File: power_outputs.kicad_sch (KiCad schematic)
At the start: 10 parts, among them Q1 BSS138, Q3 MMBT3904, Q4 MMBT3906

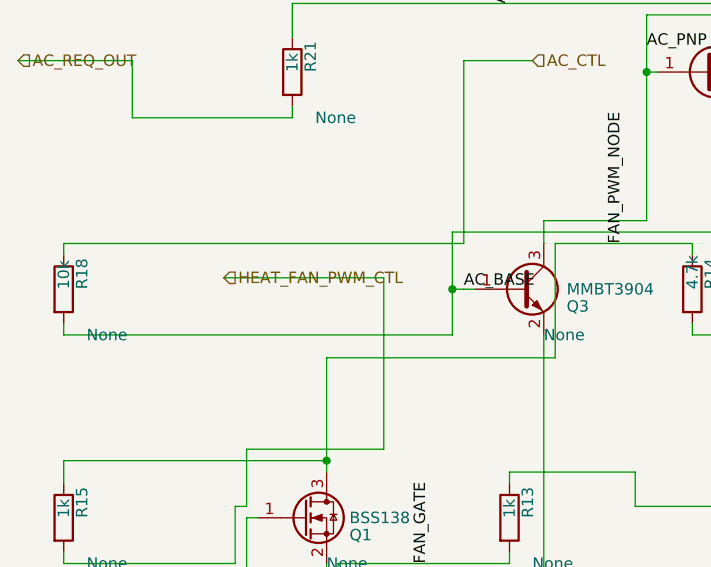
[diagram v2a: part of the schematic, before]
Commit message: optimazed load to kicad
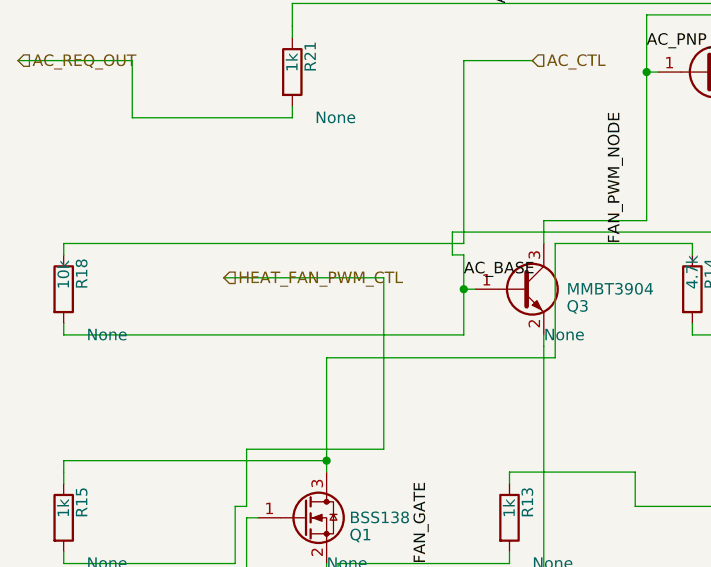
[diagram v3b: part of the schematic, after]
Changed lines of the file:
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@@
 		(instances
 			(project "Untitled"
-				(path "/1e88dd50-46bb-44a6-af8a-a123738594cb"
+				(path "/90d6963e-6ac5-4f32-9aa0-e0ee6a940a9b"
 					(reference "Q1")
 					(unit 1)
@@
 		(instances
 			(project "Untitled"
-				(path "/1e88dd50-46bb-44a6-af8a-a123738594cb"
+				(path "/90d6963e-6ac5-4f32-9aa0-e0ee6a940a9b"
 					(reference "Q3")
 					(unit 1)
@@
 		(instances
 			(project "Untitled"
-				(path "/1e88dd50-46bb-44a6-af8a-a123738594cb"
+				(path "/90d6963e-6ac5-4f32-9aa0-e0ee6a940a9b"
 					(reference "Q4")
 					(unit 1)
@@
 		(instances
 			(project "Untitled"
-				(path "/1e88dd50-46bb-44a6-af8a-a123738594cb"
+				(path "/90d6963e-6ac5-4f32-9aa0-e0ee6a940a9b"
 					(reference "R13")
 					(unit 1)
@@
 		(instances
 			(project "Untitled"
-				(path "/1e88dd50-46bb-44a6-af8a-a123738594cb"
+				(path "/90d6963e-6ac5-4f32-9aa0-e0ee6a940a9b"
 					(reference "R14")
 					(unit 1)
@@
 		(instances
 			(project "Untitled"
-				(path "/1e88dd50-46bb-44a6-af8a-a123738594cb"
+				(path "/90d6963e-6ac5-4f32-9aa0-e0ee6a940a9b"
 					(reference "R15")
 					(unit 1)
@@
 		(instances
 			(project "Untitled"
-				(path "/1e88dd50-46bb-44a6-af8a-a123738594cb"
+				(path "/90d6963e-6ac5-4f32-9aa0-e0ee6a940a9b"
 					(reference "R18")
 					(unit 1)
@@
 		(instances
 			(project "Untitled"
-				(path "/1e88dd50-46bb-44a6-af8a-a123738594cb"
+				(path "/90d6963e-6ac5-4f32-9aa0-e0ee6a940a9b"
 					(reference "R19")
 					(unit 1)
@@
 		(instances
 			(project "Untitled"
-				(path "/1e88dd50-46bb-44a6-af8a-a123738594cb"
+				(path "/90d6963e-6ac5-4f32-9aa0-e0ee6a940a9b"
 					(reference "R20")
 					(unit 1)
@@
 		(instances
 			(project "Untitled"
-				(path "/1e88dd50-46bb-44a6-af8a-a123738594cb"
+				(path "/90d6963e-6ac5-4f32-9aa0-e0ee6a940a9b"
 					(reference "R21")
 					(unit 1)
@@
 	(wire
 		(pts
-			(xy 53.34 33.02) (xy 52.07 33.02)
-		)
-		(stroke
-			(width 0)
-			(type default)
-		)
-	)
-	(wire
-		(pts
-			(xy 52.07 33.02) (xy 52.07 26.67)
+			(xy 53.34 33.02) (xy 53.34 29.21)
+		)
+		(stroke
+			(width 0)
+			(type default)
+		)
+	)
+	(wire
+		(pts
+			(xy 53.34 29.21) (xy 52.07 29.21)
+		)
+		(stroke
+			(width 0)
+			(type default)
+		)
+	)
+	(wire
+		(pts
+			(xy 52.07 29.21) (xy 52.07 26.67)
 		)
 		(stroke
@@
 	(wire
 		(pts
-			(xy 8.89 38.1) (xy 52.07 38.1)
-		)
-		(stroke
-			(width 0)
-			(type default)
-		)
-	)
-	(wire
-		(pts
-			(xy 52.07 38.1) (xy 52.07 33.02)
+			(xy 8.89 38.1) (xy 53.34 38.1)
+		)
+		(stroke
+			(width 0)
+			(type default)
+		)
+	)
+	(wire
+		(pts
+			(xy 53.34 38.1) (xy 53.34 33.02)
 		)
 		(stroke
@@
 	)
 	(junction
-		(at 52.07 33.02)
+		(at 53.34 33.02)
 		(diameter 0)
 		(color 0 0 0 0)
@@
 	)
 	(label "AC_BASE"
-		(at 53.34 33.02 180)
+		(at 53.34 31.75 180)
 		(effects
 			(font

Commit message: tests_fix
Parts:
- Q1, Q3, Q4, R13, R14, R15, R18, R19, R20, R21: hierarchy_path (none) -> /c5a034c1-1f54-4e7e-8711-0930d2b4314e/a70dfe10-e340-4dc2-93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
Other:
- title: (none) -> climate_control_niva_travel
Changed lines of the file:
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@@
 	(generator_version "9.0")
 	(paper "A4")
+	(title_block
+		(title "climate_control_niva_travel")
+	)
 	(symbol
 		(lib_id "Transistor_FET:BSS138")
@@
 			)
 		)
+		(property "hierarchy_path" "/c5a034c1-1f54-4e7e-8711-0930d2b4314e/a70dfe10-e340-4dc2-93bf-45c80fe91fa7"
+			(at 38.1 63.4999 0)
+			(effects
+				(font
+					(size 1.27 1.27)
+				)
+				(justify left)
+			)
+		)
 		(pin "1"
 		)
@@
 		)
 		(instances
-			(project "Untitled"
-				(path "/90d6963e-6ac5-4f32-9aa0-e0ee6a940a9b"
+			(project "climate_control_niva_travel"
+				(path "/c5a034c1-1f54-4e7e-8711-0930d2b4314e/a70dfe10-e340-4dc2-93bf-45c80fe91fa7"
 					(reference "Q1")
 					(unit 1)
@@
 			)
 		)
+		(property "hierarchy_path" "/c5a034c1-1f54-4e7e-8711-0930d2b4314e/a70dfe10-e340-4dc2-93bf-45c80fe91fa7"
+			(at 62.23 38.0999 0)
+			(effects
+				(font
+					(size 1.27 1.27)
+				)
+				(justify left)
+			)
+		)
 		(pin "1"
 		)
@@
 		)
 		(instances
-			(project "Untitled"
-				(path "/90d6963e-6ac5-4f32-9aa0-e0ee6a940a9b"
+			(project "climate_control_niva_travel"
+				(path "/c5a034c1-1f54-4e7e-8711-0930d2b4314e/a70dfe10-e340-4dc2-93bf-45c80fe91fa7"
 					(reference "Q3")
 					(unit 1)
@@
 			)
 		)
+		(property "hierarchy_path" "/c5a034c1-1f54-4e7e-8711-0930d2b4314e/a70dfe10-e340-4dc2-93bf-45c80fe91fa7"
+			(at 82.55 13.9699 0)
+			(effects
+				(font
+					(size 1.27 1.27)
+				)
+				(justify left)
+			)
+		)
 		(pin "1"
 		)
@@
 		)
 		(instances
-			(project "Untitled"
-				(path "/90d6963e-6ac5-4f32-9aa0-e0ee6a940a9b"
+			(project "climate_control_niva_travel"
+				(path "/c5a034c1-1f54-4e7e-8711-0930d2b4314e/a70dfe10-e340-4dc2-93bf-45c80fe91fa7"
 					(reference "Q4")
 					(unit 1)
@@
 			)
 		)
+		(property "hierarchy_path" "/c5a034c1-1f54-4e7e-8711-0930d2b4314e/a70dfe10-e340-4dc2-93bf-45c80fe91fa7"
+			(at 60.96 63.4999 0)
+			(effects
+				(font
+					(size 1.27 1.27)
+				)
+				(justify left)
+			)
+		)
 		(pin "1"
 		)
@@
 		)
 		(instances
-			(project "Untitled"
-				(path "/90d6963e-6ac5-4f32-9aa0-e0ee6a940a9b"
+			(project "climate_control_niva_travel"
+				(path "/c5a034c1-1f54-4e7e-8711-0930d2b4314e/a70dfe10-e340-4dc2-93bf-45c80fe91fa7"
 					(reference "R13")
 					(unit 1)
@@
 			)
 		)
+		(property "hierarchy_path" "/c5a034c1-1f54-4e7e-8711-0930d2b4314e/a70dfe10-e340-4dc2-93bf-45c80fe91fa7"
+			(at 81.28 38.0999 0)
+			(effects
+				(font
+					(size 1.27 1.27)
+				)
+				(justify left)
+			)
+		)
 		(pin "1"
 		)
@@
 		)
 		(instances
-			(project "Untitled"
-				(path "/90d6963e-6ac5-4f32-9aa0-e0ee6a940a9b"
+			(project "climate_control_niva_travel"
+				(path "/c5a034c1-1f54-4e7e-8711-0930d2b4314e/a70dfe10-e340-4dc2-93bf-45c80fe91fa7"
 					(reference "R14")
 					(unit 1)
@@
 			)
 		)
+		(property "hierarchy_path" "/c5a034c1-1f54-4e7e-8711-0930d2b4314e/a70dfe10-e340-4dc2-93bf-45c80fe91fa7"
+			(at 11.43 63.4999 0)
+			(effects
+				(font
+					(size 1.27 1.27)
+				)
+				(justify left)
+			)
+		)
 		(pin "1"
 		)
@@
 		)
 		(instances
-			(project "Untitled"
-				(path "/90d6963e-6ac5-4f32-9aa0-e0ee6a940a9b"
+			(project "climate_control_niva_travel"
+				(path "/c5a034c1-1f54-4e7e-8711-0930d2b4314e/a70dfe10-e340-4dc2-93bf-45c80fe91fa7"
 					(reference "R15")
 					(unit 1)
@@
 			)
 		)
+		(property "hierarchy_path" "/c5a034c1-1f54-4e7e-8711-0930d2b4314e/a70dfe10-e340-4dc2-93bf-45c80fe91fa7"
+			(at 11.43 38.0999 0)
+			(effects
+				(font
+					(size 1.27 1.27)
+				)
+				(justify left)
+			)
+		)
 		(pin "1"
 		)
@@
 		)
 		(instances
-			(project "Untitled"
-				(path "/90d6963e-6ac5-4f32-9aa0-e0ee6a940a9b"
+			(project "climate_control_niva_travel"
+				(path "/c5a034c1-1f54-4e7e-8711-0930d2b4314e/a70dfe10-e340-4dc2-93bf-45c80fe91fa7"
 					(reference "R18")
 					(unit 1)
@@
 			)
 		)
+		(property "hierarchy_path" "/c5a034c1-1f54-4e7e-8711-0930d2b4314e/a70dfe10-e340-4dc2-93bf-45c80fe91fa7"
+			(at 100.33 38.0999 0)
+			(effects
+				(font
+					(size 1.27 1.27)
+				)
+				(justify left)
+			)
+		)
 		(pin "1"
 		)
@@
 		)
 		(instances
-			(project "Untitled"
-				(path "/90d6963e-6ac5-4f32-9aa0-e0ee6a940a9b"
+			(project "climate_control_niva_travel"
+				(path "/c5a034c1-1f54-4e7e-8711-0930d2b4314e/a70dfe10-e340-4dc2-93bf-45c80fe91fa7"
 					(reference "R19")
 					(unit 1)
@@
 			)
 		)
+		(property "hierarchy_path" "/c5a034c1-1f54-4e7e-8711-0930d2b4314e/a70dfe10-e340-4dc2-93bf-45c80fe91fa7"
+			(at 100.33 13.9699 0)
+			(effects
+				(font
+					(size 1.27 1.27)
+				)
+				(justify left)
+			)
+		)
 		(pin "1"
 		)
@@
 		)
 		(instances
-			(project "Untitled"
-				(path "/90d6963e-6ac5-4f32-9aa0-e0ee6a940a9b"
+			(project "climate_control_niva_travel"
+				(path "/c5a034c1-1f54-4e7e-8711-0930d2b4314e/a70dfe10-e340-4dc2-93bf-45c80fe91fa7"
 					(reference "R20")
 					(unit 1)
@@
 			)
 		)
+		(property "hierarchy_path" "/c5a034c1-1f54-4e7e-8711-0930d2b4314e/a70dfe10-e340-4dc2-93bf-45c80fe91fa7"
+			(at 36.83 13.9699 0)
+			(effects
+				(font
+					(size 1.27 1.27)
+				)
+				(justify left)
+			)
+		)
 		(pin "1"
 		)
@@
 		)
 		(instances
-			(project "Untitled"
-				(path "/90d6963e-6ac5-4f32-9aa0-e0ee6a940a9b"
+			(project "climate_control_niva_travel"
+				(path "/c5a034c1-1f54-4e7e-8711-0930d2b4314e/a70dfe10-e340-4dc2-93bf-45c80fe91fa7"
 					(reference "R21")
 					(unit 1)
@@
 	(junction
 		(at 73.66 8.89)
+		(diameter 0)
+		(color 0 0 0 0)
+	)
+	(junction
+		(at 49.53 63.5)
+		(diameter 0)
+		(color 0 0 0 0)
+	)
+	(junction
+		(at 71.12 27.94)
+		(diameter 0)
+		(color 0 0 0 0)
+	)
+	(junction
+		(at 53.34 31.75)
+		(diameter 0)
+		(color 0 0 0 0)
+	)
+	(junction
+		(at 73.66 6.35)
+		(diameter 0)
+		(color 0 0 0 0)
+	)
+	(junction
+		(at 58.42 1.27)
 		(diameter 0)
 		(color 0 0 0 0)
@@
 	)
 	(hierarchical_label "AC_REQ_OUT"
-		(shape input)
+		(shape output)
 		(at 3.81 7.62 0)
 		(effects
@@
 	)
 	(hierarchical_label "HEAT_FAN_PWM_CTL"
-		(shape input)
+		(shape output)
 		(at 26.67 31.75 0)
 		(effects

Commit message: refactoring
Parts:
- Q1, Q3, Q4, R13, R14, R15, R18, R19, R20, R21: hierarchy_path /c5a034c1-1f54-4e7e-8711-0930d2b4314e/a70dfe10-e340-4dc2-93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 -> (none)
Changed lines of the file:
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@@
-			)
-		)
-		(property "hierarchy_path" "/c5a034c1-1f54-4e7e-8711-0930d2b4314e/a70dfe10-e340-4dc2-93bf-45c80fe91fa7"
-			(at 38.1 63.4999 0)
-			(effects
-				(font
-					(size 1.27 1.27)
-				)
-				(justify left)
 			)
 		)
@@
 		(instances
 			(project "climate_control_niva_travel"
-				(path "/c5a034c1-1f54-4e7e-8711-0930d2b4314e/a70dfe10-e340-4dc2-93bf-45c80fe91fa7"
-					(reference "Q1")
+				(path "/165a98f1-2dde-4141-9fdc-c935d39c8cff/176bfc83-1f39-4dbb-bd36-1c3de8b994cb/"
+					(reference "Q0701")
 					(unit 1)
 				)
@@
 			)
 		)
-		(property "hierarchy_path" "/c5a034c1-1f54-4e7e-8711-0930d2b4314e/a70dfe10-e340-4dc2-93bf-45c80fe91fa7"
-			(at 62.23 38.0999 0)
-			(effects
-				(font
-					(size 1.27 1.27)
-				)
-				(justify left)
-			)
-		)
 		(pin "1"
 		)
@@
 		(instances
 			(project "climate_control_niva_travel"
-				(path "/c5a034c1-1f54-4e7e-8711-0930d2b4314e/a70dfe10-e340-4dc2-93bf-45c80fe91fa7"
-					(reference "Q3")
+				(path "/165a98f1-2dde-4141-9fdc-c935d39c8cff/176bfc83-1f39-4dbb-bd36-1c3de8b994cb/"
+					(reference "Q0703")
 					(unit 1)
 				)
@@
 			)
 		)
-		(property "hierarchy_path" "/c5a034c1-1f54-4e7e-8711-0930d2b4314e/a70dfe10-e340-4dc2-93bf-45c80fe91fa7"
-			(at 82.55 13.9699 0)
-			(effects
-				(font
-					(size 1.27 1.27)
-				)
-				(justify left)
-			)
-		)
 		(pin "1"
 		)
@@
 		(instances
 			(project "climate_control_niva_travel"
-				(path "/c5a034c1-1f54-4e7e-8711-0930d2b4314e/a70dfe10-e340-4dc2-93bf-45c80fe91fa7"
-					(reference "Q4")
+				(path "/165a98f1-2dde-4141-9fdc-c935d39c8cff/176bfc83-1f39-4dbb-bd36-1c3de8b994cb/"
+					(reference "Q0704")
 					(unit 1)
 				)
@@
 			)
 		)
-		(property "hierarchy_path" "/c5a034c1-1f54-4e7e-8711-0930d2b4314e/a70dfe10-e340-4dc2-93bf-45c80fe91fa7"
-			(at 60.96 63.4999 0)
-			(effects
-				(font
-					(size 1.27 1.27)
-				)
-				(justify left)
-			)
-		)
-		(pin "1"
-		)
-		(pin "2"
-		)
-		(instances
-			(project "climate_control_niva_travel"
-				(path "/c5a034c1-1f54-4e7e-8711-0930d2b4314e/a70dfe10-e340-4dc2-93bf-45c80fe91fa7"
-					(reference "R13")
+		(pin "1"
+		)
+		(pin "2"
+		)
+		(instances
+			(project "climate_control_niva_travel"
+				(path "/165a98f1-2dde-4141-9fdc-c935d39c8cff/176bfc83-1f39-4dbb-bd36-1c3de8b994cb/"
+					(reference "R0713")
 					(unit 1)
 				)
@@
 			)
 		)
-		(property "hierarchy_path" "/c5a034c1-1f54-4e7e-8711-0930d2b4314e/a70dfe10-e340-4dc2-93bf-45c80fe91fa7"
-			(at 81.28 38.0999 0)
-			(effects
-				(font
-					(size 1.27 1.27)
-				)
-				(justify left)
-			)
-		)
-		(pin "1"
-		)
-		(pin "2"
-		)
-		(instances
-			(project "climate_control_niva_travel"
-				(path "/c5a034c1-1f54-4e7e-8711-0930d2b4314e/a70dfe10-e340-4dc2-93bf-45c80fe91fa7"
-					(reference "R14")
+		(pin "1"
+		)
+		(pin "2"
+		)
+		(instances
+			(project "climate_control_niva_travel"
+				(path "/165a98f1-2dde-4141-9fdc-c935d39c8cff/176bfc83-1f39-4dbb-bd36-1c3de8b994cb/"
+					(reference "R0714")
 					(unit 1)
 				)
@@
 			)
 		)
-		(property "hierarchy_path" "/c5a034c1-1f54-4e7e-8711-0930d2b4314e/a70dfe10-e340-4dc2-93bf-45c80fe91fa7"
-			(at 11.43 63.4999 0)
-			(effects
-				(font
-					(size 1.27 1.27)
-				)
-				(justify left)
-			)
-		)
-		(pin "1"
-		)
-		(pin "2"
-		)
-		(instances
-			(project "climate_control_niva_travel"
-				(path "/c5a034c1-1f54-4e7e-8711-0930d2b4314e/a70dfe10-e340-4dc2-93bf-45c80fe91fa7"
-					(reference "R15")
+		(pin "1"
+		)
+		(pin "2"
+		)
+		(instances
+			(project "climate_control_niva_travel"
+				(path "/165a98f1-2dde-4141-9fdc-c935d39c8cff/176bfc83-1f39-4dbb-bd36-1c3de8b994cb/"
+					(reference "R0715")
 					(unit 1)
 				)
@@
 			)
 		)
-		(property "hierarchy_path" "/c5a034c1-1f54-4e7e-8711-0930d2b4314e/a70dfe10-e340-4dc2-93bf-45c80fe91fa7"
-			(at 11.43 38.0999 0)
-			(effects
-				(font
-					(size 1.27 1.27)
-				)
-				(justify left)
-			)
-		)
-		(pin "1"
-		)
-		(pin "2"
-		)
-		(instances
-			(project "climate_control_niva_travel"
-				(path "/c5a034c1-1f54-4e7e-8711-0930d2b4314e/a70dfe10-e340-4dc2-93bf-45c80fe91fa7"
-					(reference "R18")
+		(pin "1"
+		)
+		(pin "2"
+		)
+		(instances
+			(project "climate_control_niva_travel"
+				(path "/165a98f1-2dde-4141-9fdc-c935d39c8cff/176bfc83-1f39-4dbb-bd36-1c3de8b994cb/"
+					(reference "R0718")
 					(unit 1)
 				)
@@
 			)
 		)
-		(property "hierarchy_path" "/c5a034c1-1f54-4e7e-8711-0930d2b4314e/a70dfe10-e340-4dc2-93bf-45c80fe91fa7"
-			(at 100.33 38.0999 0)
-			(effects
-				(font
-					(size 1.27 1.27)
-				)
-				(justify left)
-			)
-		)
-		(pin "1"
-		)
-		(pin "2"
-		)
-		(instances
-			(project "climate_control_niva_travel"
-				(path "/c5a034c1-1f54-4e7e-8711-0930d2b4314e/a70dfe10-e340-4dc2-93bf-45c80fe91fa7"
-					(reference "R19")
+		(pin "1"
+		)
+		(pin "2"
+		)
+		(instances
+			(project "climate_control_niva_travel"
+				(path "/165a98f1-2dde-4141-9fdc-c935d39c8cff/176bfc83-1f39-4dbb-bd36-1c3de8b994cb/"
+					(reference "R0719")
 					(unit 1)
 				)
@@
 			)
 		)
-		(property "hierarchy_path" "/c5a034c1-1f54-4e7e-8711-0930d2b4314e/a70dfe10-e340-4dc2-93bf-45c80fe91fa7"
-			(at 100.33 13.9699 0)
-			(effects
-				(font
-					(size 1.27 1.27)
-				)
-				(justify left)
-			)
-		)
-		(pin "1"
-		)
-		(pin "2"
-		)
-		(instances
-			(project "climate_control_niva_travel"
-				(path "/c5a034c1-1f54-4e7e-8711-0930d2b4314e/a70dfe10-e340-4dc2-93bf-45c80fe91fa7"
-					(reference "R20")
+		(pin "1"
+		)
+		(pin "2"
+		)
+		(instances
+			(project "climate_control_niva_travel"
+				(path "/165a98f1-2dde-4141-9fdc-c935d39c8cff/176bfc83-1f39-4dbb-bd36-1c3de8b994cb/"
+					(reference "R0720")
 					(unit 1)
 				)
@@
 			)
 		)
-		(property "hierarchy_path" "/c5a034c1-1f54-4e7e-8711-0930d2b4314e/a70dfe10-e340-4dc2-93bf-45c80fe91fa7"
-			(at 36.83 13.9699 0)
-			(effects
-				(font
-					(size 1.27 1.27)
-				)
-				(justify left)
-			)
-		)
-		(pin "1"
-		)
-		(pin "2"
-		)
-		(instances
-			(project "climate_control_niva_travel"
-				(path "/c5a034c1-1f54-4e7e-8711-0930d2b4314e/a70dfe10-e340-4dc2-93bf-45c80fe91fa7"
-					(reference "R21")
-					(unit 1)
-				)
+		(pin "1"
+		)
+		(pin "2"
+		)
+		(instances
+			(project "climate_control_niva_travel"
+				(path "/165a98f1-2dde-4141-9fdc-c935d39c8cff/176bfc83-1f39-4dbb-bd36-1c3de8b994cb/"
+					(reference "R0721")
+					(unit 1)
+				)
